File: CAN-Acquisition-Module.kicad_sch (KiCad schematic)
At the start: 0 parts

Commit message: Rev.A2 pretty much finished
V USB bypasses inductor L2
Srew terminal pin holes size reduced
Thermally isolated SHT3x
Fixed U1 footprint
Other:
- sheet Screen ports: added none; removed SCREEN_RESET
- note added: "--- Revision History --- A1: Initial release A2: - VUSB bypasses inductor L2 - Reduce screw terminal hole size - Thermally isolate SHT3x - U1 footprint fix"
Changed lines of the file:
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@@
     (comment 1 "Designer: Hugo Boyce")
   )
-  (junction (at 185.42 76.2) (diameter 0) (color 0 0 0 0)
-  )
   (wire (pts (xy 59.69 57.15) (xy 73.66 57.15))
     (stroke (width 0) (type default) (color 0 0 0 0))
@@
     (stroke (width 0) (type default) (color 0 0 0 0))
   )
-  (wire (pts (xy 198.12 76.2) (xy 185.42 76.2))
-    (stroke (width 0) (type default) (color 0 0 0 0))
-  )
   (wire (pts (xy 109.22 39.37) (xy 109.22 41.91))
     (stroke (width 0) (type default) (color 0 0 0 0))
@@
   (wire (pts (xy 129.54 100.33) (xy 129.54 129.54))
     (stroke (width 0) (type default) (color 0 0 0 0))
+  )
+  (text "--- Revision History ---\nA1: Initial release\nA2:\n- VUSB bypasses inductor L2\n- Reduce screw terminal hole size\n- Thermally isolate SHT3x \n- U1 footprint fix"
+    (at 16.51 185.42 0)
+    (effects (font (size 1.27 1.27)) (justify left bottom))
   )
   (label "ADC10" (at 129.54 129.54 0)
@@
     )
     (pin "SCREEN_SS" input (at 198.12 59.69 180)
-      (effects (font (size 1.27 1.27)) (justify left))
-    )
-    (pin "SCREEN_RESET" input (at 198.12 76.2 180)
       (effects (font (size 1.27 1.27)) (justify left))
     )
@@
       (reference "R45") (unit 1) (value "Ω") (footprint "Resistor_SMD:R_0603_1608Metric")
     )
-    (path "/5f5345ca-f2d2-466f-a4ac-3c846c4226e8/958d8bf1-ac9b-4596-9de4-94b09e72356a"
-      (reference "R46") (unit 1) (value "Ω") (footprint "Resistor_SMD:R_0603_1608Metric")
-    )
-    (path "/5f5345ca-f2d2-466f-a4ac-3c846c4226e8/3df96e17-a6d1-484c-a217-02994bf396a7"
-      (reference "R47") (unit 1) (value "0 Ω") (footprint "Resistor_SMD:R_0603_1608Metric")
-    )
-    (path "/5f5345ca-f2d2-466f-a4ac-3c846c4226e8/3d025a35-ec4f-4c66-88db-fa668b95a8c1"
-      (reference "R48") (unit 1) (value "0 Ω") (footprint "Resistor_SMD:R_0603_1608Metric")
-    )
-    (path "/5f5345ca-f2d2-466f-a4ac-3c846c4226e8/bc272525-76ab-46c7-bfd5-1729544cf1d6"
-      (reference "R49") (unit 1) (value "Ω") (footprint "Resistor_SMD:R_0603_1608Metric")
-    )
     (path "/5f5345ca-f2d2-466f-a4ac-3c846c4226e8/538d7447-2814-4dcb-aa5b-dc482cea4c84"
       (reference "R50") (unit 1) (value "1 kΩ") (footprint "Resistor_SMD:R_0603_1608Metric")
@@
       (reference "R72") (unit 1) (value "10 kΩ") (footprint "Resistor_SMD:R_0603_1608Metric")
     )
-    (path "/6d7c7c9c-1e38-4555-8d83-d2635ba71983/cf9d4249-7694-4ef8-8dcb-8fe2f55de202"
-      (reference "R73") (unit 1) (value "Ω") (footprint "Resistor_SMD:R_0603_1608Metric")
-    )
     (path "/a7ab022e-987c-4858-83e2-b4df42ea9922/0e1ecc51-c7e2-4c5b-be2f-5772e6393294"

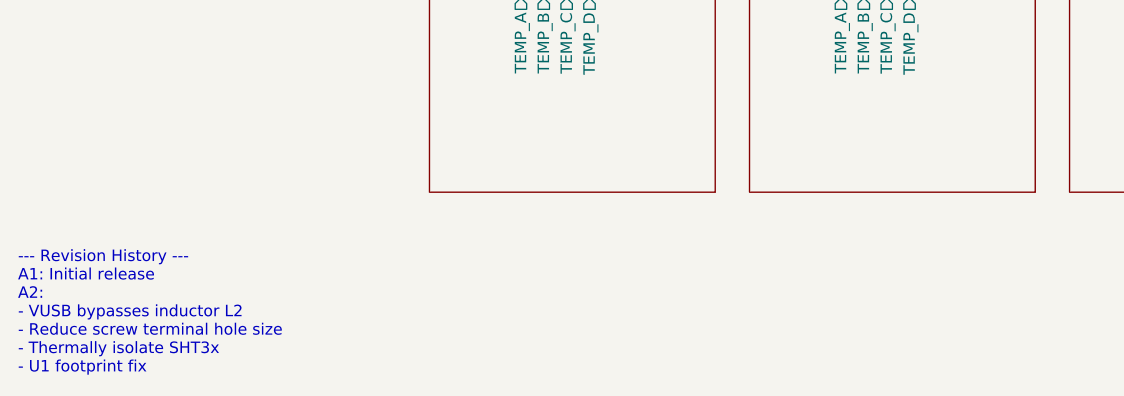
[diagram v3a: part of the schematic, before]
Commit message: Changed 47uF cap to 4.7uF
Filtration can be done in software instead of hardware
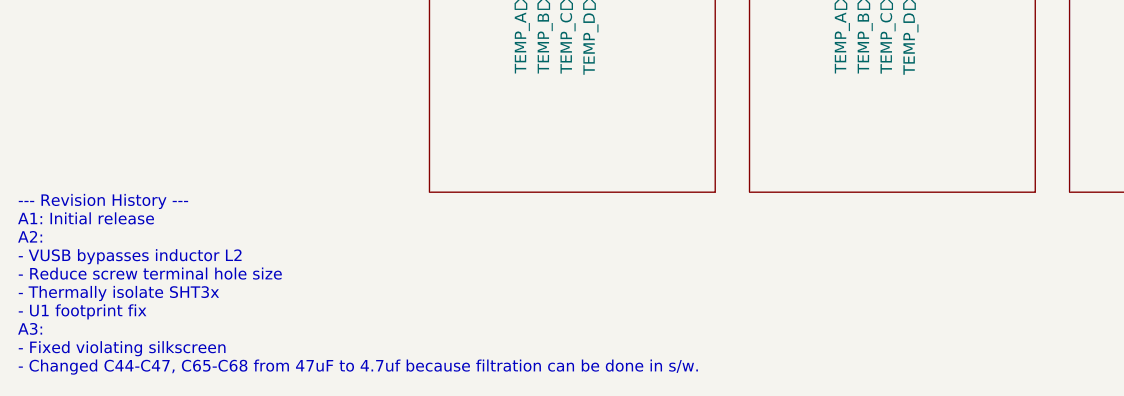
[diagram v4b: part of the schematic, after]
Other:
- note added: "--- Revision History --- A1: Initial release A2: - VUSB bypasses inductor L2 - Reduce screw terminal hole size - Thermally isolate SHT3x - U1 footprint fix A3: - Fixed violating silkscreen - Changed C44-C47, C65-C68 from 47uF to 4.7uf because filtration can be done in s/w."
- note removed: "--- Revision History --- A1: Initial release A2: - VUSB bypasses inductor L2 - Reduce screw terminal hole size - Thermally isolate SHT3x - U1 footprint fix"
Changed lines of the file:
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@@
     (stroke (width 0) (type default) (color 0 0 0 0))
   )
-  (text "--- Revision History ---\nA1: Initial release\nA2:\n- VUSB bypasses inductor L2\n- Reduce screw terminal hole size\n- Thermally isolate SHT3x \n- U1 footprint fix"
+  (text "--- Revision History ---\nA1: Initial release\nA2:\n- VUSB bypasses inductor L2\n- Reduce screw terminal hole size\n- Thermally isolate SHT3x \n- U1 footprint fix\nA3:\n- Fixed violating silkscreen\n- Changed C44-C47, C65-C68 from 47uF to 4.7uf because filtration can be done in s/w.\n"
     (at 16.51 185.42 0)
     (effects (font (size 1.27 1.27)) (justify left bottom))
@@
     )
     (path "/71359799-714b-4644-8db4-495310f76a1b/7004cdd7-3681-4bf3-9e76-794f5450a63a"
-      (reference "C44") (unit 1) (value "47 uF") (footprint "Capacitor_SMD:C_1206_3216Metric")
+      (reference "C44") (unit 1) (value "4.7 uF") (footprint "Capacitor_SMD:C_1206_3216Metric")
     )
     (path "/71359799-714b-4644-8db4-495310f76a1b/f08dfbd8-2dec-44ae-b168-2f2708e1aa24"
-      (reference "C45") (unit 1) (value "47 uF") (footprint "Capacitor_SMD:C_1206_3216Metric")
+      (reference "C45") (unit 1) (value "4.7 uF") (footprint "Capacitor_SMD:C_1206_3216Metric")
     )
     (path "/71359799-714b-4644-8db4-495310f76a1b/45ca6ada-6f1e-4756-b08c-de2fea6d5903"
-      (reference "C46") (unit 1) (value "47 uF") (footprint "Capacitor_SMD:C_1206_3216Metric")
+      (reference "C46") (unit 1) (value "4.7 uF") (footprint "Capacitor_SMD:C_1206_3216Metric")
     )
     (path "/71359799-714b-4644-8db4-495310f76a1b/95ca51fd-e4e0-4028-8ae9-68556ba9b26b"
-      (reference "C47") (unit 1) (value "47 uF") (footprint "Capacitor_SMD:C_1206_3216Metric")
+      (reference "C47") (unit 1) (value "4.7 uF") (footprint "Capacitor_SMD:C_1206_3216Metric")
     )
     (path "/5f5345ca-f2d2-466f-a4ac-3c846c4226e8/959fe419-961a-4323-b067-cdd3d4e5cd29"
@@
     )
     (path "/a7ab022e-987c-4858-83e2-b4df42ea9922/7004cdd7-3681-4bf3-9e76-794f5450a63a"
-      (reference "C65") (unit 1) (value "47 uF") (footprint "Capacitor_SMD:C_1206_3216Metric")
+      (reference "C65") (unit 1) (value "4.7 uF") (footprint "Capacitor_SMD:C_1206_3216Metric")
     )
     (path "/a7ab022e-987c-4858-83e2-b4df42ea9922/f08dfbd8-2dec-44ae-b168-2f2708e1aa24"
-      (reference "C66") (unit 1) (value "47 uF") (footprint "Capacitor_SMD:C_1206_3216Metric")
+      (reference "C66") (unit 1) (value "4.7 uF") (footprint "Capacitor_SMD:C_1206_3216Metric")
     )
     (path "/a7ab022e-987c-4858-83e2-b4df42ea9922/45ca6ada-6f1e-4756-b08c-de2fea6d5903"
-      (reference "C67") (unit 1) (value "47 uF") (footprint "Capacitor_SMD:C_1206_3216Metric")
+      (reference "C67") (unit 1) (value "4.7 uF") (footprint "Capacitor_SMD:C_1206_3216Metric")
     )
     (path "/a7ab022e-987c-4858-83e2-b4df42ea9922/95ca51fd-e4e0-4028-8ae9-68556ba9b26b"
-      (reference "C68") (unit 1) (value "47 uF") (footprint "Capacitor_SMD:C_1206_3216Metric")
+      (reference "C68") (unit 1) (value "4.7 uF") (footprint "Capacitor_SMD:C_1206_3216Metric")
     )
     (path "/00000000-0000-0000-0000-0000628fba98/c1b863f4-d8a3-46b3-b82c-8bba37961f44"

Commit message: Added differential BOM for order (to be removed later)
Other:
- note added: "--- Revision History --- A1: Initial release A2: - VUSB bypasses inductor L2 - Reduce screw terminal hole size - Thermally isolate SHT3x - U1 footprint fix A3: - Fixed violating silkscreen - Added some LCSC part numbers - Changed C44-C47, C65-C68 from 47uF to 4.7uf because filtration can be done in s/w."
- note removed: "--- Revision History --- A1: Initial release A2: - VUSB bypasses inductor L2 - Reduce screw terminal hole size - Thermally isolate SHT3x - U1 footprint fix A3: - Fixed violating silkscreen - Changed C44-C47, C65-C68 from 47uF to 4.7uf because filtration can be done in s/w."
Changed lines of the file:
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@@
     (stroke (width 0) (type default) (color 0 0 0 0))
   )
-  (text "--- Revision History ---\nA1: Initial release\nA2:\n- VUSB bypasses inductor L2\n- Reduce screw terminal hole size\n- Thermally isolate SHT3x \n- U1 footprint fix\nA3:\n- Fixed violating silkscreen\n- Changed C44-C47, C65-C68 from 47uF to 4.7uf because filtration can be done in s/w.\n"
+  (text "--- Revision History ---\nA1: Initial release\nA2:\n- VUSB bypasses inductor L2\n- Reduce screw terminal hole size\n- Thermally isolate SHT3x \n- U1 footprint fix\nA3:\n- Fixed violating silkscreen\n- Added some LCSC part numbers\n- Changed C44-C47, C65-C68 from 47uF to 4.7uf because filtration can be done in s/w.\n"
     (at 16.51 185.42 0)
     (effects (font (size 1.27 1.27)) (justify left bottom))
@@
     )
     (path "/6a23b5b9-2864-4994-bd7a-8563b9182093/bfac1122-ceea-4c6d-944c-ae41c70eefa5"
-      (reference "U5") (unit 1) (value "SN65HVD234") (footprint "Package_SO:SOIC-8_3.9x4.9mm_P1.27mm")
+      (reference "U5") (unit 1) (value "SN65HVD235") (footprint "Package_SO:SOIC-8_3.9x4.9mm_P1.27mm")
     )
     (path "/71359799-714b-4644-8db4-495310f76a1b/91ded3ad-ffd9-462d-bc57-c7590de3347b"

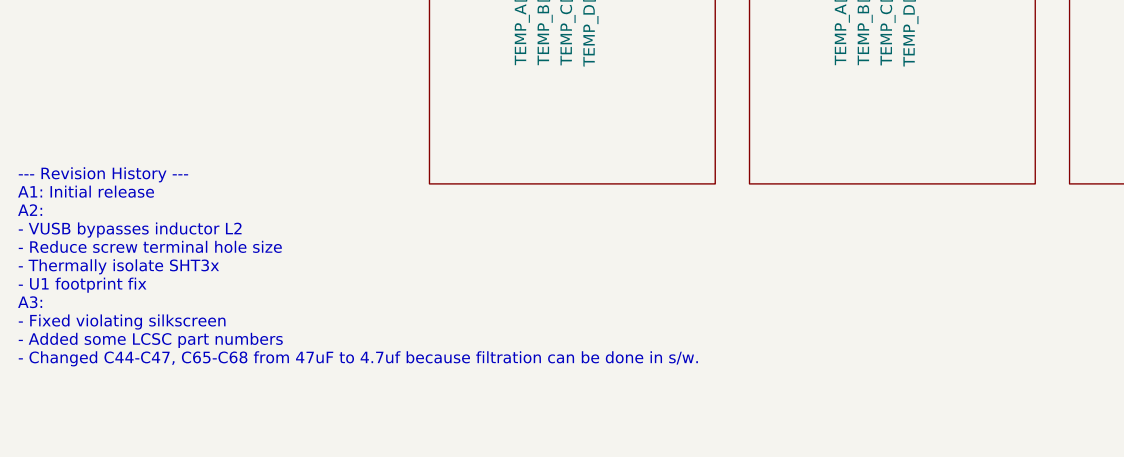
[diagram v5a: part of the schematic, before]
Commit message: Created Rev B1
Replaced buck regulator S-8581AA with AP63200 because of shortage
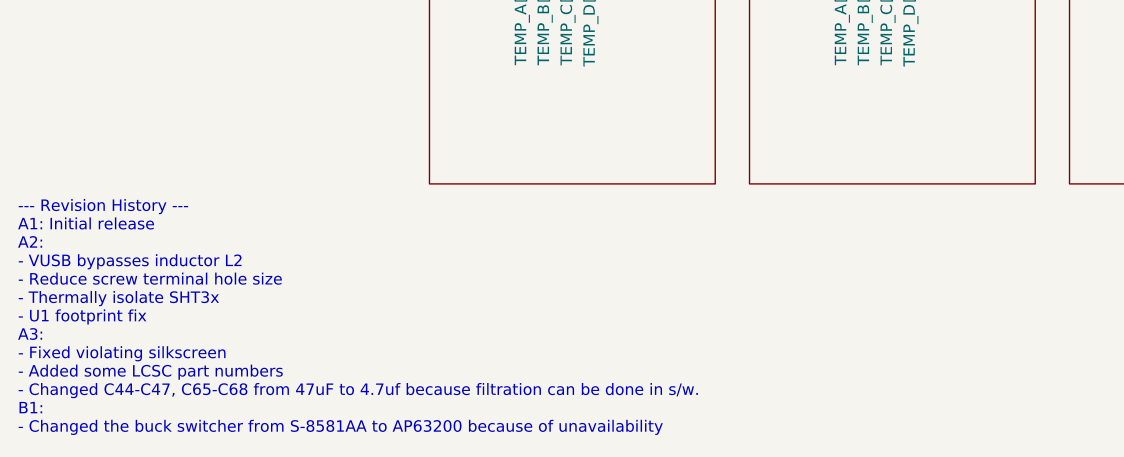
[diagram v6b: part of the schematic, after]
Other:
- note added: "--- Revision History --- A1: Initial release A2: - VUSB bypasses inductor L2 - Reduce screw terminal hole size - Thermally isolate SHT3x - U1 footprint fix A3: - Fixed violating silkscreen - Added some LCSC part numbers - Changed C44-C47, C65-C68 from 47uF to 4.7uf because filtration can be done in s/w. B1: - Changed the buck switcher from S-8581AA to AP63200 because of unavailability"
- note removed: "--- Revision History --- A1: Initial release A2: - VUSB bypasses inductor L2 - Reduce screw terminal hole size - Thermally isolate SHT3x - U1 footprint fix A3: - Fixed violating silkscreen - Added some LCSC part numbers - Changed C44-C47, C65-C68 from 47uF to 4.7uf because filtration can be done in s/w."
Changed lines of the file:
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@@
     (stroke (width 0) (type default) (color 0 0 0 0))
   )
-  (text "--- Revision History ---\nA1: Initial release\nA2:\n- VUSB bypasses inductor L2\n- Reduce screw terminal hole size\n- Thermally isolate SHT3x \n- U1 footprint fix\nA3:\n- Fixed violating silkscreen\n- Added some LCSC part numbers\n- Changed C44-C47, C65-C68 from 47uF to 4.7uf because filtration can be done in s/w.\n"
-    (at 16.51 185.42 0)
+  (text "--- Revision History ---\nA1: Initial release\nA2:\n- VUSB bypasses inductor L2\n- Reduce screw terminal hole size\n- Thermally isolate SHT3x \n- U1 footprint fix\nA3:\n- Fixed violating silkscreen\n- Added some LCSC part numbers\n- Changed C44-C47, C65-C68 from 47uF to 4.7uf because filtration can be done in s/w.\nB1:\n- Changed the buck switcher from S-8581AA to AP63200 because of unavailability"
+    (at 16.51 193.04 0)
     (effects (font (size 1.27 1.27)) (justify left bottom))
   )
@@
       (reference "#PWR022") (unit 1) (value "GND") (footprint "")
     )
-    (path "/00000000-0000-0000-0000-0000628fba98/76677108-2d86-40df-8da8-3adc1b48b568"
-      (reference "#PWR023") (unit 1) (value "GND") (footprint "")
-    )
     (path "/00000000-0000-0000-0000-0000628fba98/a44a161f-59e8-4a07-bda9-a9f7ef5f0a45"
       (reference "#PWR024") (unit 1) (value "GND") (footprint "")
     )
-    (path "/00000000-0000-0000-0000-0000628fba98/632a14c4-5418-41de-8bdb-5fb2d71f0eb0"
-      (reference "#PWR025") (unit 1) (value "GND") (footprint "")
-    )
     (path "/00000000-0000-0000-0000-0000628fba98/e99bd506-f24e-431f-b2ff-be9b37c274e1"
       (reference "#PWR026") (unit 1) (value "VBUS") (footprint "")
@@
       (reference "C8") (unit 1) (value "100 nF") (footprint "Capacitor_SMD:C_0603_1608Metric")
     )
-    (path "/00000000-0000-0000-0000-0000628fba98/d5058c67-b3f8-4ce2-b079-04b7c813c1f7"
-      (reference "C9") (unit 1) (value "1 uF") (footprint "Capacitor_SMD:C_0603_1608Metric")
+    (path "/00000000-0000-0000-0000-0000628fba98/57217b3d-ea71-41cb-b42e-2d16385a35c0"
+      (reference "C9") (unit 1) (value "100 nF") (footprint "Capacitor_SMD:C_0603_1608Metric")
     )
     (path "/00000000-0000-0000-0000-0000628fba98/3164e408-fd78-4800-8190-1f71e5f46e9c"
       (reference "C10") (unit 1) (value "4.7 uF") (footprint "Capacitor_SMD:C_1206_3216Metric")
     )
-    (path "/00000000-0000-0000-0000-0000628fba98/bef2da02-8637-419f-aa56-8ca839c90801"
-      (reference "C11") (unit 1) (value "33 pF") (footprint "Capacitor_SMD:C_0603_1608Metric")
+    (path "/00000000-0000-0000-0000-0000628fba98/ebb98d33-c041-4cc2-915f-f7d313945072"
+      (reference "C11") (unit 1) (value "47 pF") (footprint "Capacitor_SMD:C_0603_1608Metric")
     )
     (path "/00000000-0000-0000-0000-0000628fba98/c5afc38f-6d76-4442-b66e-a96e615f68b6"
@@
       (reference "L2") (unit 1) (value "470 uH") (footprint "CAN-Acquisition-Module:Murata_LQH43_1812(4532_Metric)")
     )
-    (path "/00000000-0000-0000-0000-0000628fba98/f1815cfb-946b-45e1-985b-8e0ed5e489f3"
-      (reference "L3") (unit 1) (value "4.7 uH") (footprint "Inductor_SMD:L_1008_2520Metric")
+    (path "/00000000-0000-0000-0000-0000628fba98/b63a63c6-3569-4d11-9c51-0d08b6e3afab"
+      (reference "L3") (unit 1) (value "6.8 uH") (footprint "CAN-Acquisition-Module:Murata_LQH3_1212(3030_Metric)")
     )
     (path "/00000000-0000-0000-0000-0000628fa103/00000000-0000-0000-0000-000062a18c81"
@@
     )
     (path "/00000000-0000-0000-0000-0000628fba98/d211914c-1b58-429d-a5af-715028c1a46e"
-      (reference "R8") (unit 1) (value "47 kΩ") (footprint "Resistor_SMD:R_0603_1608Metric")
-    )
-    (path "/00000000-0000-0000-0000-0000628fba98/bb37d496-e761-4ef3-bef0-688ba9e9bb7c"
-      (reference "R9") (unit 1) (value "15 kΩ") (footprint "Resistor_SMD:R_0603_1608Metric")
+      (reference "R8") (unit 1) (value "18.2 kΩ") (footprint "Resistor_SMD:R_0603_1608Metric")
+    )
+    (path "/00000000-0000-0000-0000-0000628fba98/5b1d0791-c9c8-475c-9bc2-489348ee00a7"
+      (reference "R9") (unit 1) (value "6.2 kΩ") (footprint "Resistor_SMD:R_0805_2012Metric")
     )
     (path "/00000000-0000-0000-0000-0000628fa103/e3b2b661-117a-4ce1-8c99-8ba64393126c"
@@
       (reference "R19") (unit 1) (value "Ω") (footprint "Resistor_SMD:R_0603_1608Metric")
     )
-    (path "/6a23b5b9-2864-4994-bd7a-8563b9182093/f4e8f079-13e2-474d-b2a5-b77899afb5ca"
-      (reference "R20") (unit 1) (value "22 kΩ") (footprint "Resistor_SMD:R_0603_1608Metric")
+    (path "/6a23b5b9-2864-4994-bd7a-8563b9182093/21f6975f-0eb3-4988-a59b-86a1a79a7d24"
+      (reference "R20") (unit 1) (value "18.2 kΩ") (footprint "Resistor_SMD:R_0603_1608Metric")
     )
     (path "/6a23b5b9-2864-4994-bd7a-8563b9182093/1cf81b43-2c10-41da-9491-13a80c1363a9"
@@
       (reference "U1") (unit 1) (value "AZ431LAN") (footprint "Package_TO_SOT_SMD:SOT-23")
     )
-    (path "/00000000-0000-0000-0000-0000628fba98/1e04a080-bbaf-4b74-9a27-2d4ce3bbc20d"
-      (reference "U2") (unit 1) (value "S-8581AA") (footprint "CAN-Acquisition-Module:Ablic_HSTN-8-A")
+    (path "/00000000-0000-0000-0000-0000628fba98/a965ceb8-8aca-4c71-b50d-dcb1cce225e4"
+      (reference "U2") (unit 1) (value "AP63200") (footprint "CAN-Acquisition-Module:Diodes-Inc_TSOT26")
     )
     (path "/00000000-0000-0000-0000-0000628fa103/00000000-0000-0000-0000-0000628f5983"
